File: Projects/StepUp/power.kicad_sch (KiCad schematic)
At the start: 53 parts, among them J10 Conn_01x02, J6 Conn_01x02, J7 Conn_01x02, J8 Conn_01x02, J9 Conn_01x02, Q3 BSS83P, Q4 BSS83P, U5 MCP73832T-2ACI_OT, U6 NCP1117-3.3_SOT223, U7 MIC2253

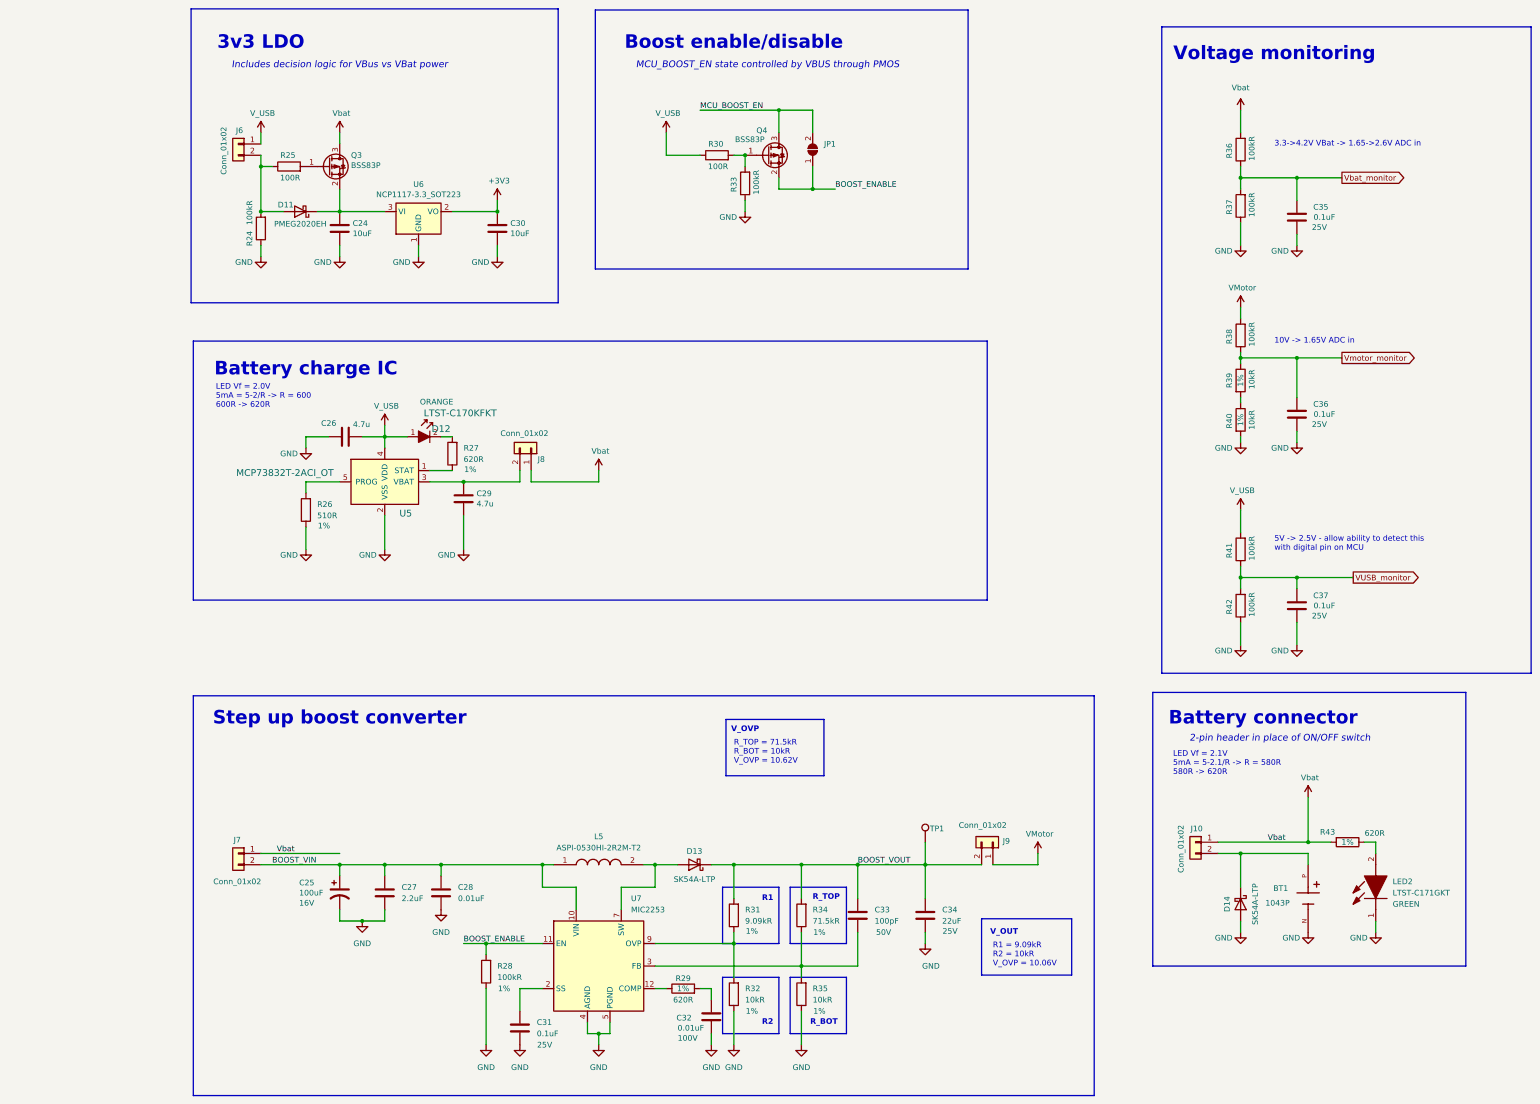
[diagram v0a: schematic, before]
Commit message: chore(pins): MCU_BOOST_EN to MCU, fixed errors
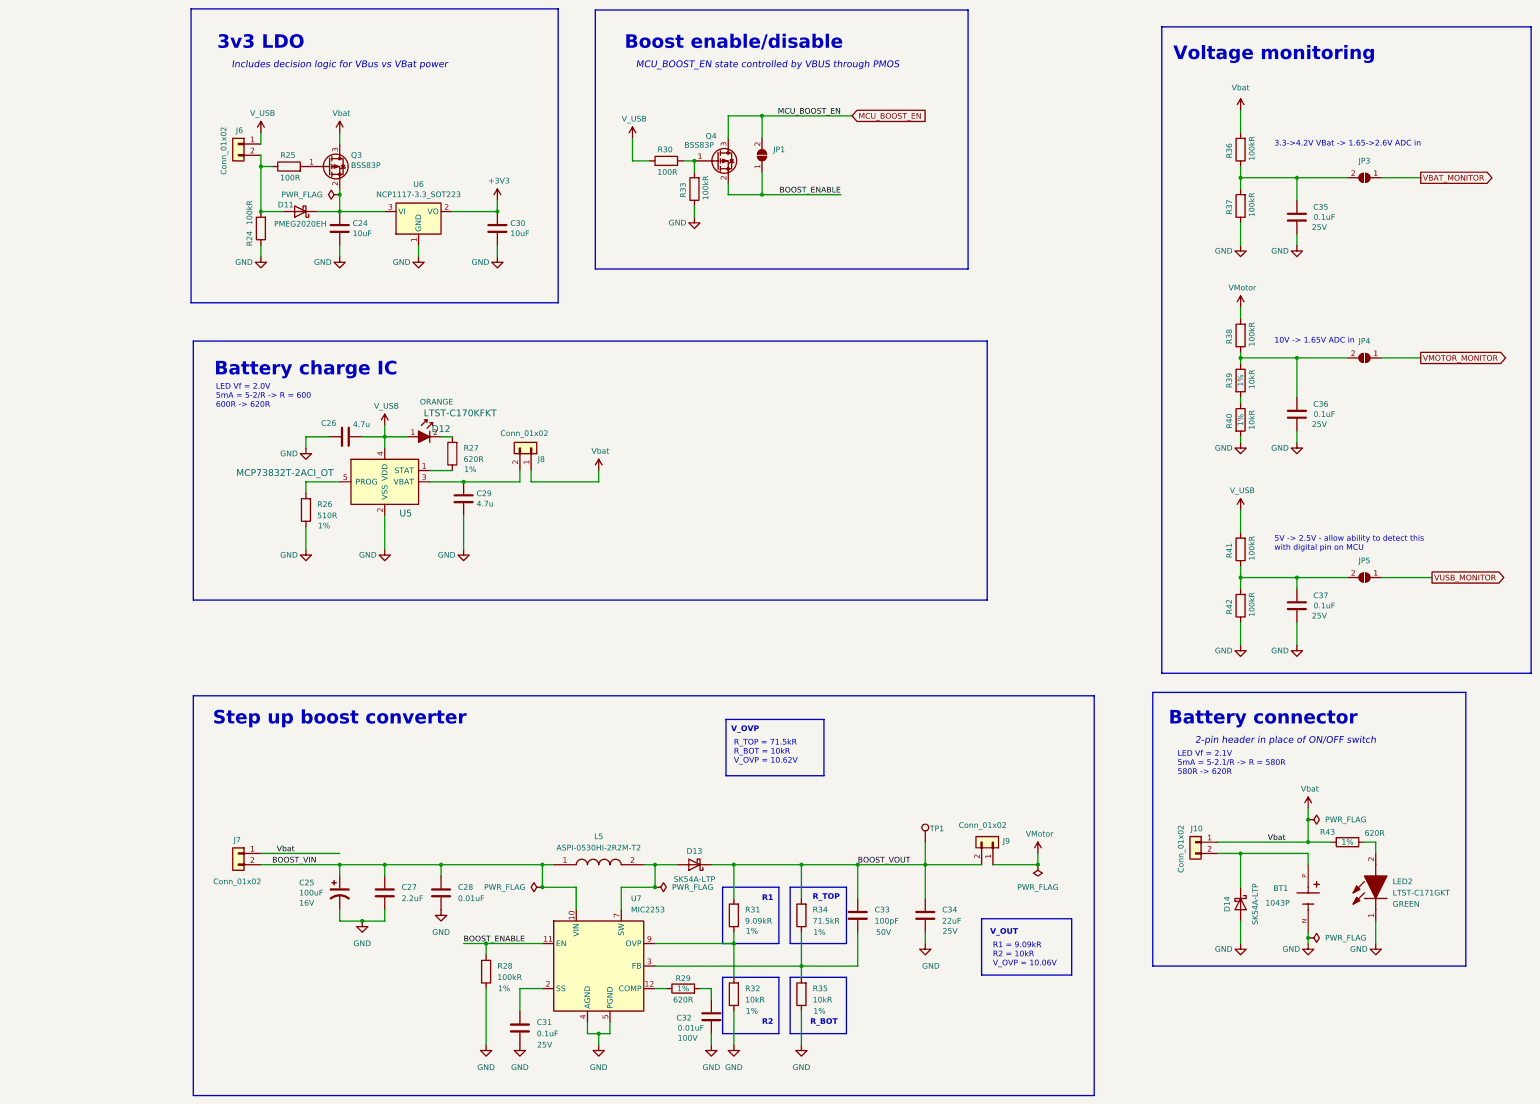
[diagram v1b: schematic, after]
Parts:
- added JP3, JP4, JP5: SolderJumper_2_Open, Jumper:SolderJumper-2_P1.3mm_Open_RoundedPad1.0x1.5mm, symbol Jumper:SolderJumper_2_Open
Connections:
- net VUSB_monitor: no longer names the net of C37.2, R41.1, R42.2
- net VUSB_monitor: now also JP5.2 (B)
- net Vbat_monitor: no longer names the net of C35.2, R36.1, R37.2
- net Vbat_monitor: now also JP3.2 (B)
- net Vmotor_monitor: no longer names the net of C36.2, R38.1, R39.1
- net Vmotor_monitor: now also JP4.2 (B)
- new net VBAT_MONITOR: JP3.1 (A)
- new net VMOTOR_MONITOR: JP4.1 (A)
- new net VUSB_MONITOR: JP5.1 (A)
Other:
- moved on the sheet: JP1, Q4, R30, R33

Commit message: feat(layout): Blocks organised
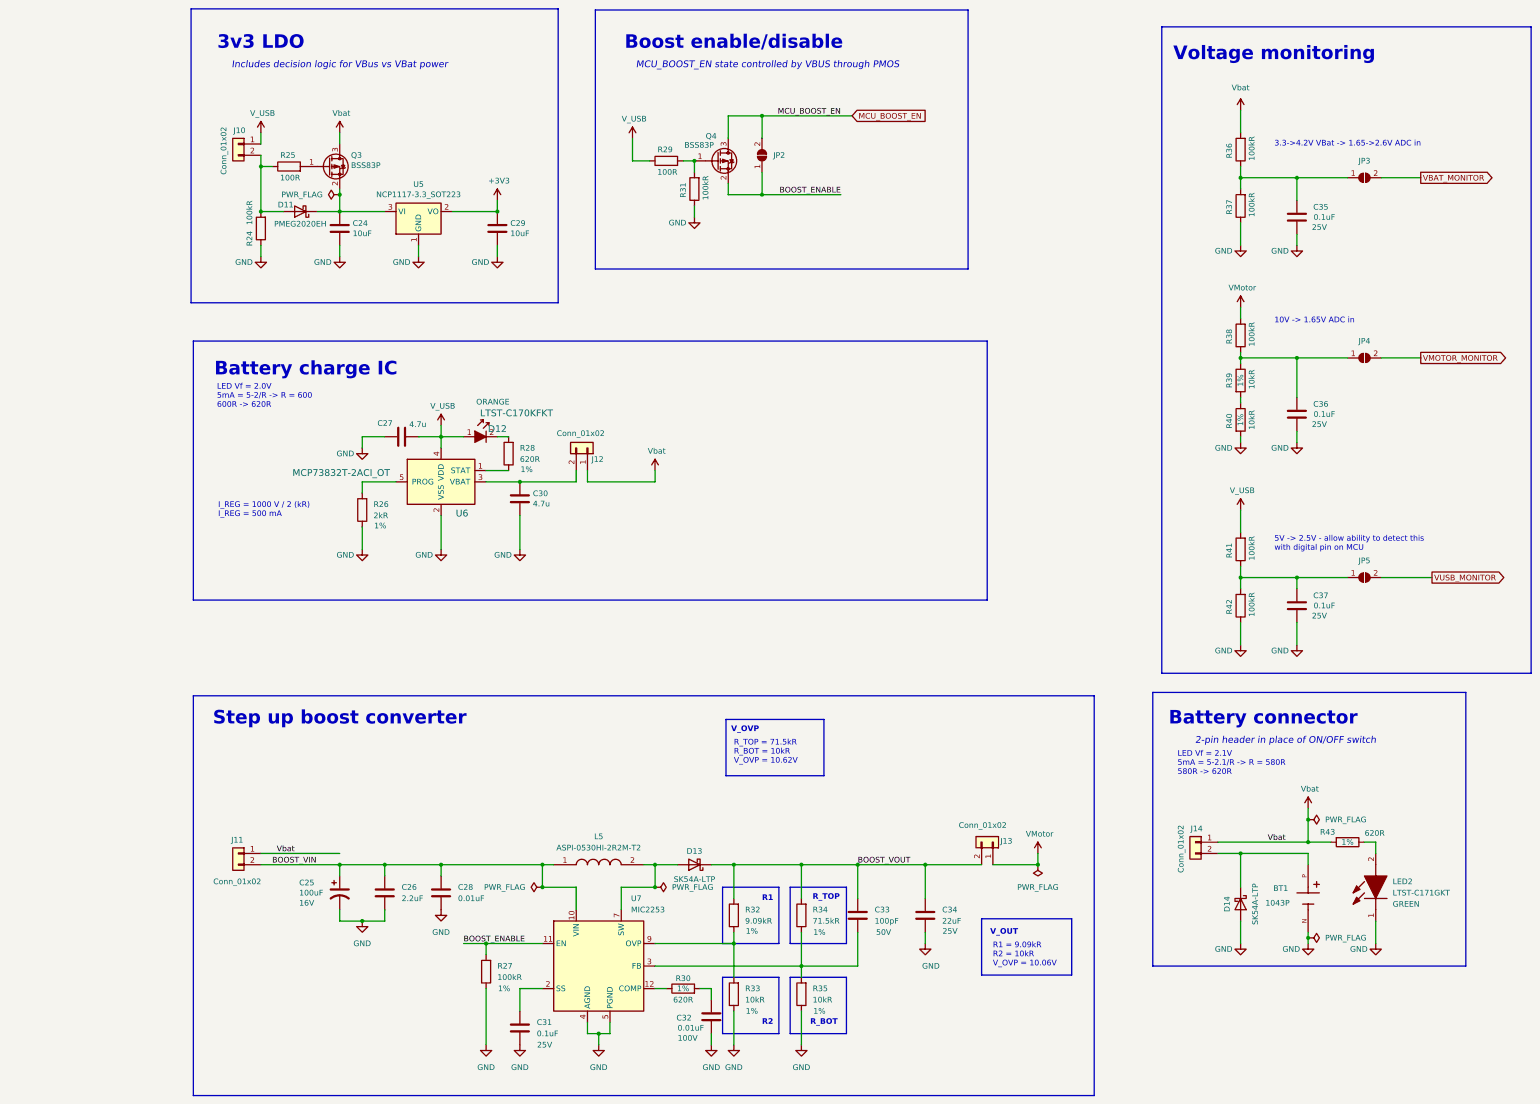
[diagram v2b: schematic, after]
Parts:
- removed JP1: SolderJumper_2_Open, Jumper:SolderJumper-2_P1.3mm_Open_RoundedPad1.0x1.5mm, symbol Jumper:SolderJumper_2_Open
- removed TP1: TestPoint, TestPoint:TestPoint_Pad_D1.5mm, symbol Connector:TestPoint
- added JP2: SolderJumper_2_Open, Jumper:SolderJumper-2_P1.3mm_Open_RoundedPad1.0x1.5mm, symbol Jumper:SolderJumper_2_Open
- R26: value 510R -> 2kR
- renumbered C27 to C26, C26 to C27, C30 to C29, C29 to C30, J6 to J10, J7 to J11, J8 to J12, J9 to J13, J10 to J14, R28 to R27, R27 to R28, R30 to R29, R29 to R30, R33 to R31, R31 to R32, R32 to R33, U6 to U5, U5 to U6
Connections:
- net BOOST_ENABLE: now also JP2.1 (A)
- net MCU_BOOST_EN: now also JP2.2 (B)
- net VBAT_MONITOR: now also JP3.2 (B); no longer JP3.1 (A)
- net VMOTOR_MONITOR: now also JP4.2 (B); no longer JP4.1 (A)
- net VUSB_MONITOR: now also JP5.2 (B); no longer JP5.1 (A)
- net at C37.2, R41.1, R42.2: now also JP5.1 (A); no longer JP5.2 (B)
- net at C35.2, R36.1, R37.2: now also JP3.1 (A); no longer JP3.2 (B)
- net at C36.2, R38.1, R39.1: now also JP4.1 (A); no longer JP4.2 (B)
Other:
- note added: "I_REG = 1000 V / 2 (kR) I_REG = 500 mA"
- moved on the sheet: C27, C30, D12, J12, R26, R28, U6

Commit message: feat(tidy): Bigger PMOS, added footprints
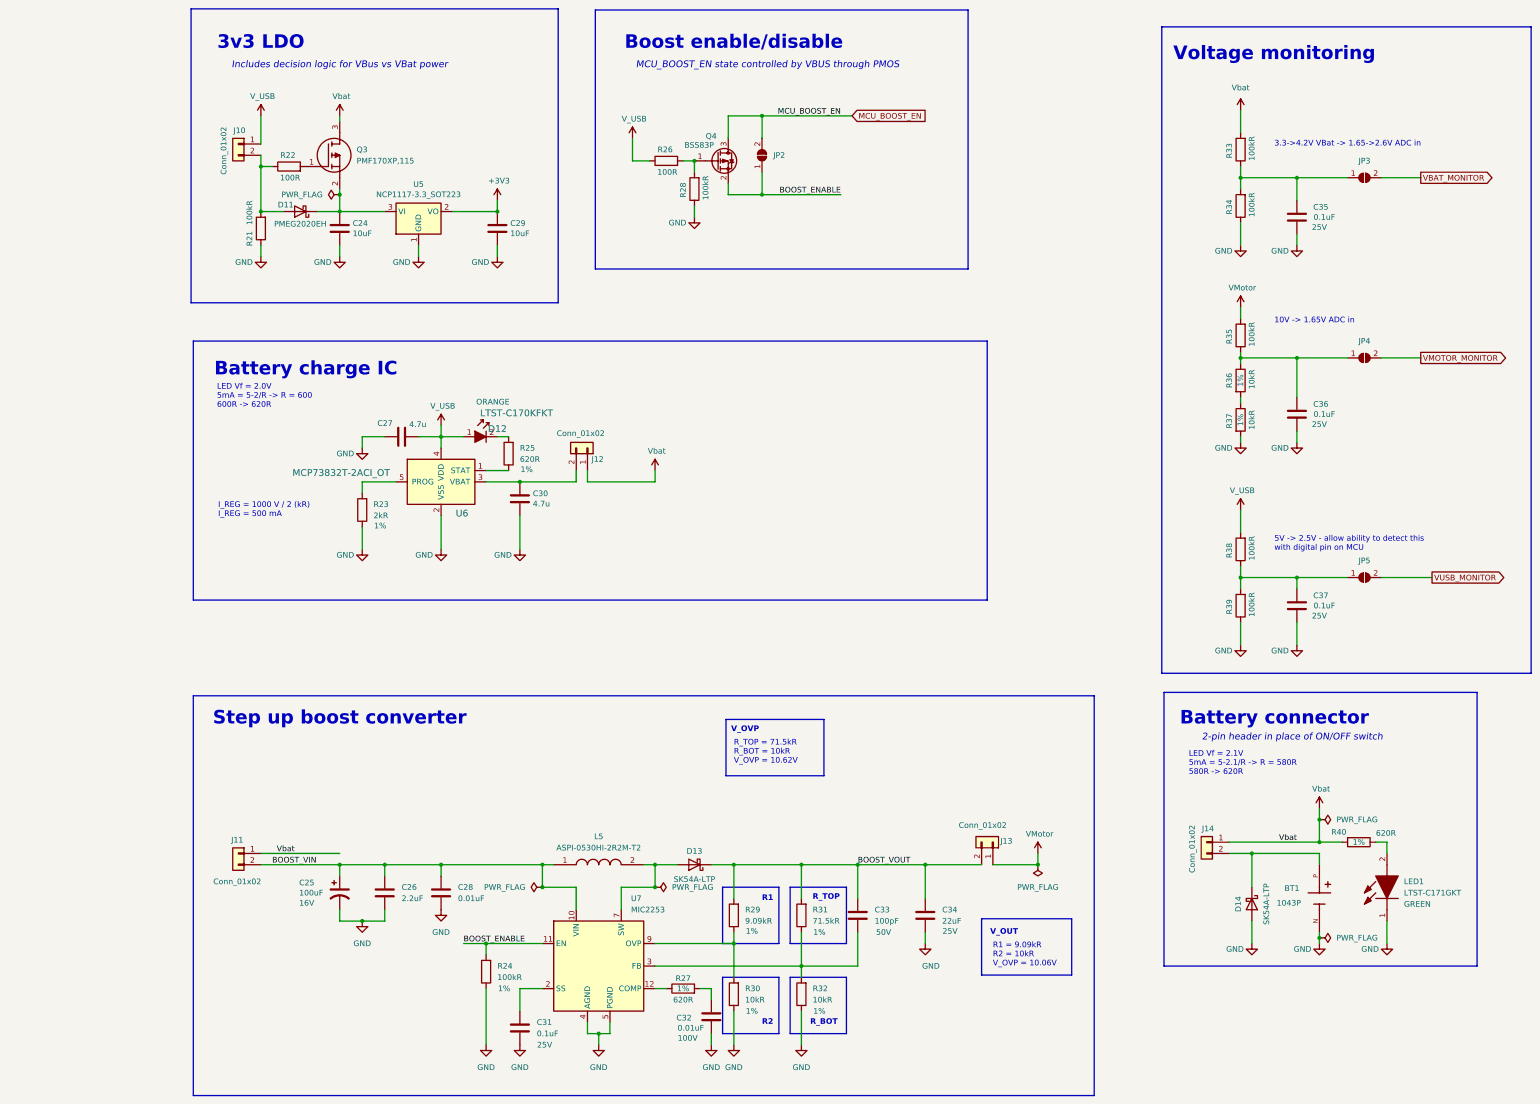
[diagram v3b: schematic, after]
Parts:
- removed Q3: BSS83P, Package_TO_SOT_SMD:SOT-23, symbol Transistor_FET:BSS83P
- added Q3: PMF170XP,115, Samacsys:SOT65P210X110-3N, symbol Samacsys:PMF170XP,115
- renumbered LED2 to LED1, R24 to R21, R25 to R22, R26 to R23, R27 to R24, R28 to R25, R29 to R26, R30 to R27, R31 to R28, R32 to R29, R33 to R30, R34 to R31, R35 to R32, R36 to R33, R37 to R34, R38 to R35, R39 to R36, R40 to R37, R41 to R38, R42 to R39, R43 to R40
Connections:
- net Vbat: now also Q3.3 (D)
- net at R22.2: now also Q3.1 (G)
- net at C24.1, D11.1 (K), U5.3 (VI): now also Q3.2 (S)
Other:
- moved on the sheet: BT1, D14, J14, LED1, R40

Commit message: feat(layout): TMC & Boost layout begin
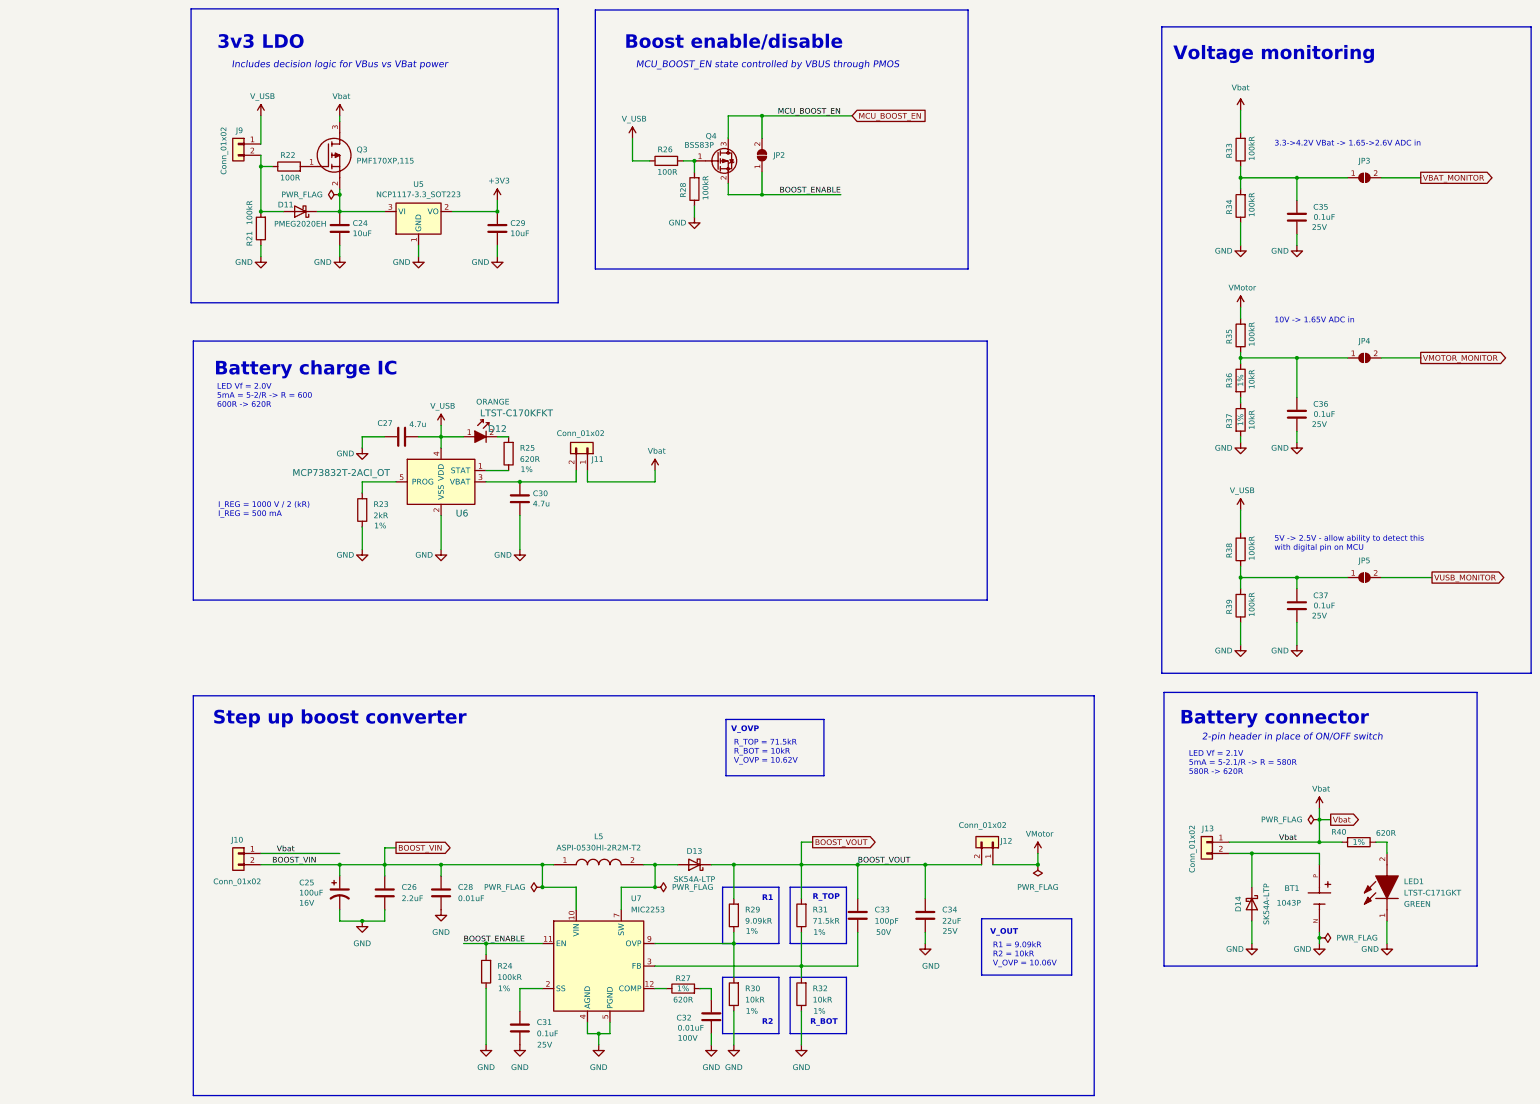
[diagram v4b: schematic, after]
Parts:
- renumbered J11 to J10, J12 to J11, J13 to J12, J14 to J13, J10 to J9
